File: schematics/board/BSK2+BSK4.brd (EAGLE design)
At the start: 82 x 100 mm, 44 parts

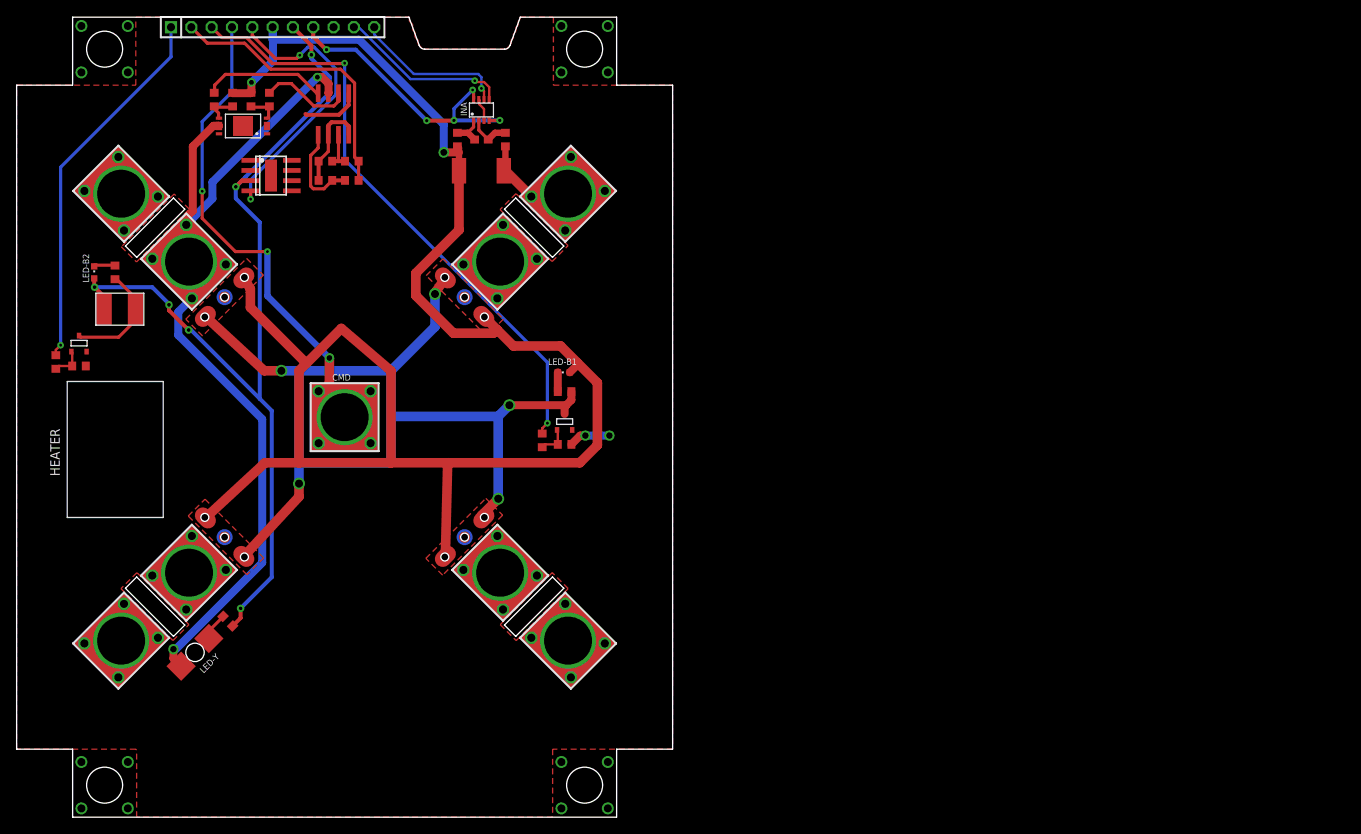
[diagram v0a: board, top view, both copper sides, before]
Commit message: Исправлены площадки механизмов Розе, соответствующие платы и герберы плат
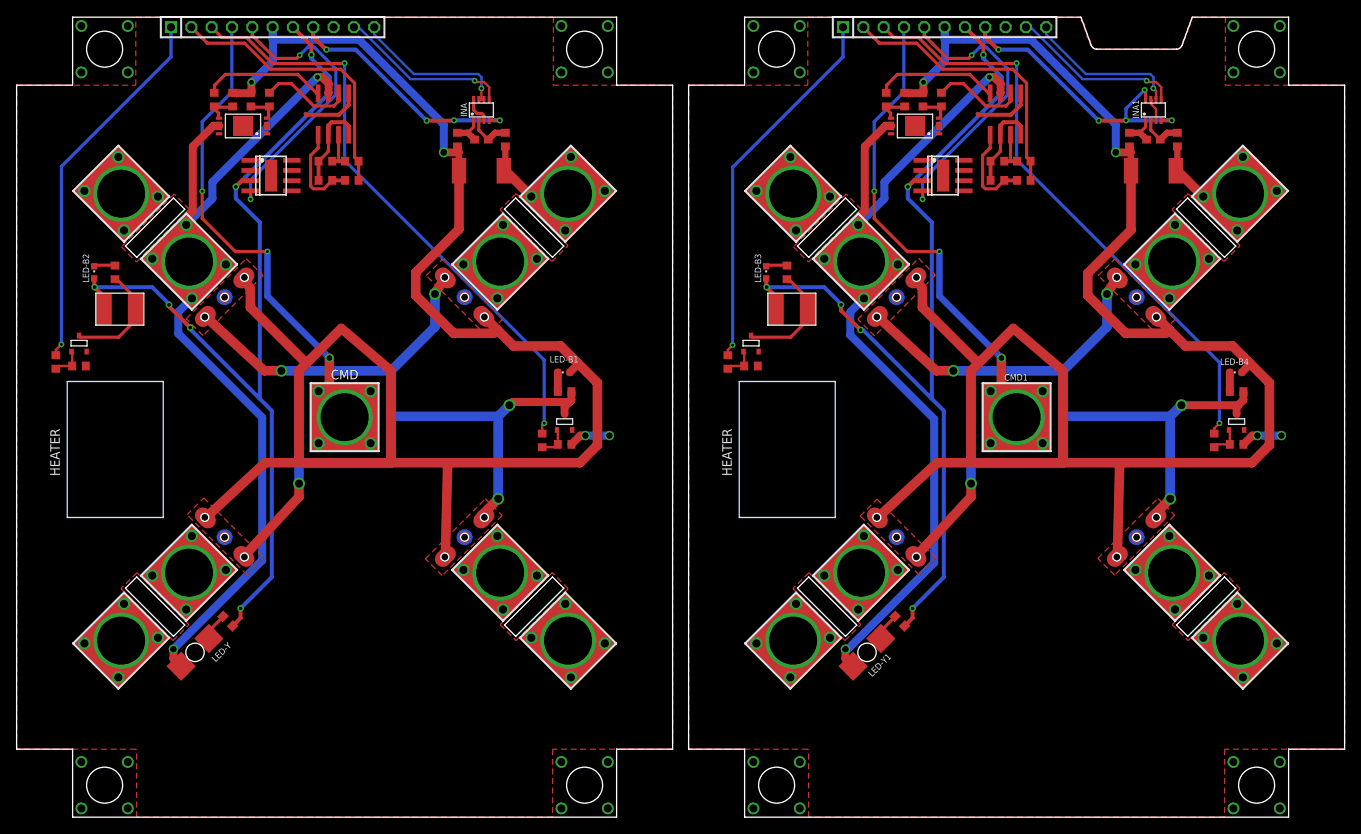
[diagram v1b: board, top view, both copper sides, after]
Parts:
- added BKU1: (no value), pinheadCS:1X11
- added C1: 0,1µ, rcl:C0603
- added CMD1: KCONNECTQUAD, CanCubeSat:KCONNECT_QUAD
- added DS18B20Z2: DS18B20Z, CanCubeSat:SOIC8+HEAT_S
- added INA1: INA219AID, CanCubeSat:SOT23-8
- added LED-B3, LED-B4: (no value), led:CHIPLED_0603
- added LED-Y1: LAP4-BOTTOM, led:P47F-BOTTOM
- added MOCD, U$27: MOCD, CanCubeSat:SOIC8
- added R10, R11: 200k, resistor:R0603
- added R15, R16, R29, R30: 100R, resistor:R0603
- added R17, R18: 100k, resistor:R0603
- added R19, R20: 2k, resistor:R0603
- added R21, R23: 1M, resistor:R0603
- added R22: 3k3, resistor:R0603
- added R24: R01, rcl:R2512
- added R25, R26: 10R, resistor:R0603
- added R27, R28: 2k26, resistor:R0603
- added U$18, U$19, U$20, U$21, U$22, U$23, U$24: KCONNECT, CanCubeSat:KCONNECT
- added U$25: FS8205A+, CanCubeSat:FS8205A+
- added U$28, U$30: SI2302CDS, CanCubeSat:SOT23-3
- added U$29: EM_HEAT, CanCubeSat:EM_HEAT
- added U$31, U$32, U$33, U$34: GRAFITGRAFIT4_2, CanCubeSat:GRAFIT4_2
- added U$35: PCB "BSK4", CanCubeSat:ITS-LOGO
- U$17: value PCB "BSK4" -> PCB "BSK2"
- U$5: value MOCD -> KCONNECT; device CanCubeSat:SOIC8 -> CanCubeSat:KCONNECT
- moved U$5 58.3 mm to (97.1, 77.9), turned to 45 degrees
- moved U$17 3.19 mm to (51.0, 9.00)
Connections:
- new net 1W1: BKU1.5, DS18B20Z2.4
- new net 3: R20.2, U$28.3, U$29.2
- new net 3V1: BKU1.8, INA1.4, INA1.8
- new net 4: R22.2, U$30.3, U$31.P$1, U$31.P$4, U$32.P$1, U$32.P$4, U$33.P$1, U$33.P$4, U$34.P$1, U$34.P$4
- new net 5V1: BKU1.7, DS18B20Z2.3, LED-B3.A, R19.1, U$29.1
- new net B2-CMD: BKU.4, CMD.1, CMD.2, CMD.3, CMD.4, CMD.P$1, CMD.P$2
- new net B2-KHEAT: BKU.1, R32.2
- new net B2-KVCC: BKU.2, R1.2, R2.2
- new net B2-ROZE: BKU.3, R3.2
- new net BUS+1: BKU1.6, LED-B4.A, R17.1, R18.2, R24.2, R25.1, U$31.P$2, U$31.P$5, U$32.P$2, U$32.P$5, U$33.P$2, U$33.P$5, U$34.P$2, U$34.P$5
- new net GND4: BKU1.9, DS18B20Z2.5, DS18B20Z2.HEAT, INA1.3, INA1.7, R10.1, R11.1, R21.2, R23.2, U$25.23, U$25.HEAT, U$27.2, U$27.4, U$27.5, U$28.2, U$30.2
- new net N$21: R16.1, R17.2, U$25.5
- new net N$22: R15.1, R18.1, U$25.4
- new net N$23: LED-Y1.A, R19.2
- new net N$24: LED-B3.C, R20.1
- new net N$25: LED-B4.C, R22.1
- new net N$47: C1.1, INA1.1, R25.2
- new net N$48: C1.2, INA1.2, R26.2
- new net N$49: R10.2, R27.1, U$27.1
- new net N$50: R11.2, R28.1, U$27.3
- new net N$51: R21.1, R29.1, U$28.1
- new net N$52: R23.1, R30.1, U$30.1
- new net OC2: R15.2, U$27.6
- new net OD2: R16.2, U$27.8
- new net SCL-TM1: BKU1.10, INA1.5
- new net SDA-TM1: BKU1.11, INA1.6
- new net SP+4: U$5.1, U$5.2, U$5.3, U$5.4, U$5.P$1, U$5.P$2
- new net SP+5: U$24.1, U$24.2, U$24.3, U$24.4, U$24.P$1, U$24.P$2
- new net SP+6: U$19.1, U$19.2, U$19.3, U$19.4, U$19.P$1, U$19.P$2
- new net SP+7: R24.1, R26.1, U$22.1, U$22.2, U$22.3, U$22.4, U$22.P$1, U$22.P$2
- new net SP-4: U$23.1, U$23.2, U$23.3, U$23.4, U$23.P$1, U$23.P$2
- new net SP-5: U$18.1, U$18.2, U$18.3, U$18.4, U$18.P$1, U$18.P$2
- new net SP-6: U$20.1, U$20.2, U$20.3, U$20.4, U$20.P$1, U$20.P$2
- new net SP-7: LED-Y1.C, U$21.1, U$21.2, U$21.3, U$21.4, U$21.P$1, U$21.P$2, U$25.67, U$27.7
- net 3V3: no longer INA.8
- net B4-CMD: now also BKU1.4, CMD1.1, CMD1.2, CMD1.3, CMD1.4, CMD1.P$1, CMD1.P$2; no longer BKU.4, CMD.1, CMD.2, CMD.3, CMD.4, CMD.P$1, CMD.P$2
- net B4-KHEAT: now also BKU1.1, R29.2; no longer BKU.1, R32.2
- net B4-KVCC: now also BKU1.2, R27.2, R28.2; no longer BKU.2, R1.2, R2.2
- net B4-ROZE: now also BKU1.3, R30.2; no longer BKU.3, R3.2
- net GND: now also INA.8, MOCD.2, MOCD.4, MOCD.5; no longer INA.7, U$5.2, U$5.4, U$5.5
- net N$17: now also MOCD.1; no longer U$5.1
- net N$18: now also MOCD.3; no longer U$5.3
- net OC1: now also MOCD.6; no longer U$5.6
- net OD1: now also MOCD.8; no longer U$5.8
- net SDA-TM: now also INA.7
- net SP-: now also MOCD.7; no longer U$5.7
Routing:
- net BUS+1: track 0.00 -> 221.6 mm, vias 0 -> 2
- net 4: track 0.00 -> 128.3 mm, vias 0 -> 5
- net SP-7: track 0.00 -> 125.9 mm, vias 0 -> 2
- net 5V1: track 0.00 -> 118.9 mm, vias 0 -> 6
- net B2-ROZE: track 0.00 -> 75.3 mm, vias 0 -> 2
- net B2-CMD: track 0.00 -> 75.1 mm, vias 0 -> 3
- net B2-KHEAT: track 0.00 -> 47.0 mm, vias 0 -> 1
- net 3V1: track 0.00 -> 36.2 mm, vias 0 -> 5
- net 1W1: track 0.00 -> 36.1 mm, vias 0 -> 2
- net B2-KVCC: track 0.00 -> 35.7 mm
- net SP+7: track 0.00 -> 29.9 mm
- net GND4: track 0.00 -> 26.9 mm, vias 0 -> 2
- net SP-4: track 0.00 -> 23.4 mm
- net SP-5: track 0.00 -> 23.4 mm
- net SP-6: track 0.00 -> 23.3 mm
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- added copper zone on layer 1, net GND4
- added copper zone on layer 1, net GND5
- added copper zone on layer 1, net GND6
- added copper zone on layer 1, net GND7
- added copper zone on layer 1, net HEAT4
- added copper zone on layer 1, net HEAT5
- added copper zone on layer 1, net HEAT6
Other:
- board size 82 x 100 mm -> 166 x 100 mm
